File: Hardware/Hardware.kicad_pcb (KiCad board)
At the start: 4 copper layers, 20.5 x 50.8 mm, 63 parts, among them J1 USB_C_Receptacle_USB2.0_16P, J2 PICO_PINOUT, Q1 BSS138, Q2 BSS138, U1 AP33772S, U10 TPS62933DRLR, U3 W25Q16JVUXIQ_TR, U4 RP2040, U5 AON7262E, U6 AON7262E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

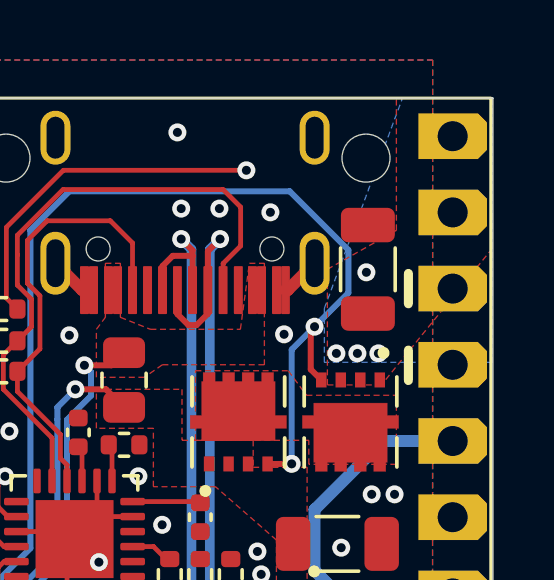
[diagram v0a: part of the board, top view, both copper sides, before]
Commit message: reduced soild copper pins to 37-40 and added high power silkscreen markings to 37-40
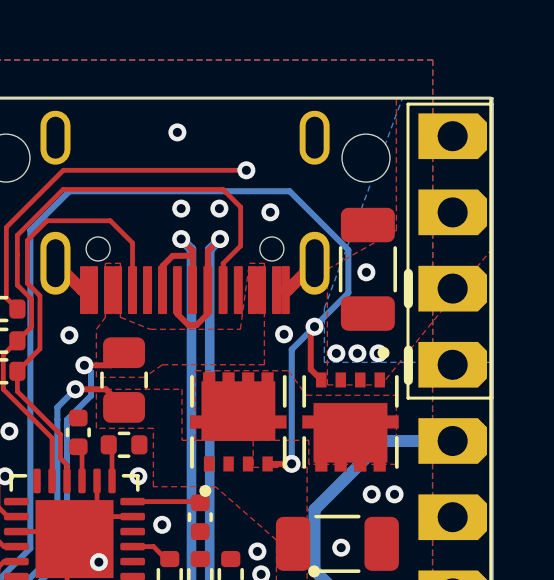
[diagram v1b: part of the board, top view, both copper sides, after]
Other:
- board text added: "GND (HP)"
- board text added: "VBUS (HP)"
- board text removed: "VBUS"
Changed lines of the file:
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@@
 			(pinfunction "3")
 			(pintype "unspecified")
-			(zone_connect 2)
 		)
 		(pad "4" thru_hole roundrect
@@
 			(pinfunction "8")
 			(pintype "unspecified")
-			(zone_connect 2)
 		)
 		(pad "9" thru_hole roundrect
@@
 			(pinfunction "13")
 			(pintype "unspecified")
-			(zone_connect 2)
 		)
 		(pad "14" thru_hole roundrect
@@
 			(pinfunction "18")
 			(pintype "unspecified")
-			(zone_connect 2)
 		)
 		(pad "19" thru_hole roundrect
@@
 			(pinfunction "23")
 			(pintype "unspecified")
-			(zone_connect 2)
 		)
 		(pad "24" thru_hole roundrect
@@
 			(pinfunction "28")
 			(pintype "unspecified")
-			(zone_connect 2)
 		)
 		(pad "29" thru_hole roundrect
@@
 			(pinfunction "33")
 			(pintype "unspecified")
-			(zone_connect 2)
 		)
 		(pad "34" thru_hole roundrect
@@
 		)
 	)
+	(gr_rect
+		(start 96.587 32.993)
+		(end 99.387 42.893)
+		(stroke
+			(width 0.1)
+			(type default)
+		)
+		(fill none)
+		(layer "B.SilkS")
+	)
 	(gr_line
 		(start 96.6 76.884)
@@
 		(layer "F.SilkS")
 	)
+	(gr_rect
+		(start 96.587 33.093)
+		(end 99.387 42.893)
+		(stroke
+			(width 0.1)
+			(type default)
+		)
+		(fill none)
+		(layer "F.SilkS")
+	)
 	(gr_line
 		(start 81.9 64.184)
@@
 		)
 	)
-	(gr_text "GND"
+	(gr_text "GND (HP)"
 		(at 96.5 39.668 0)
 		(layer "B.SilkS")
@@
 		)
 	)
-	(gr_text "VBUS"
-		(at 92.71 34.544 0)
+	(gr_text "VBUS\n(HP)"
+		(at 92.71 35.193 0)
 		(layer "B.SilkS")
 		(effects
@@
 		)
 	)
-	(gr_text "GND"
+	(gr_text "GND (HP)"
 		(at 96.4746 42.0302 0)
 		(layer "B.SilkS")
@@
 		)
 	)
-	(gr_text "VBUS"
+	(gr_text "VBUS (HP)"
 		(at 96.5 37.4074 0)
 		(layer "B.SilkS")
